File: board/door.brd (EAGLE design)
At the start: 28.8 x 37.5 mm, 15 parts, among them IC1 7805T

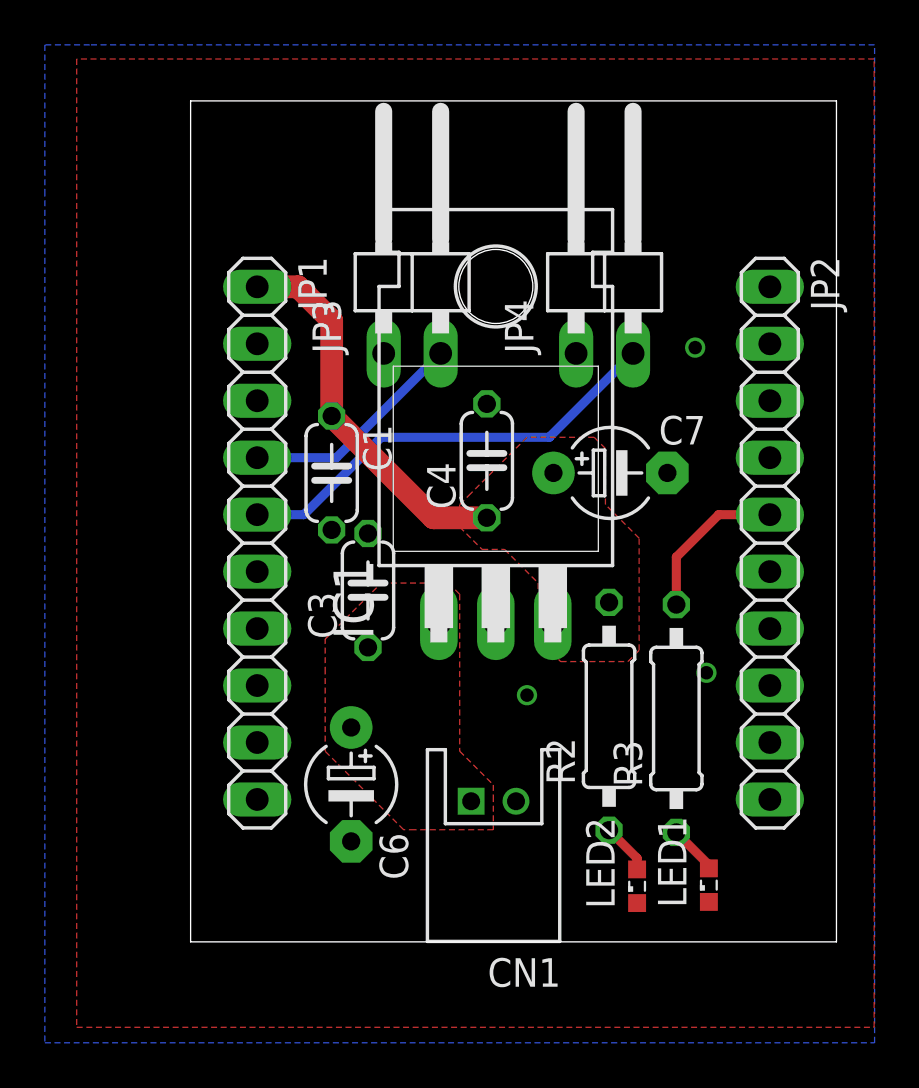
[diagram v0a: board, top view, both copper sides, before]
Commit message: add user_button
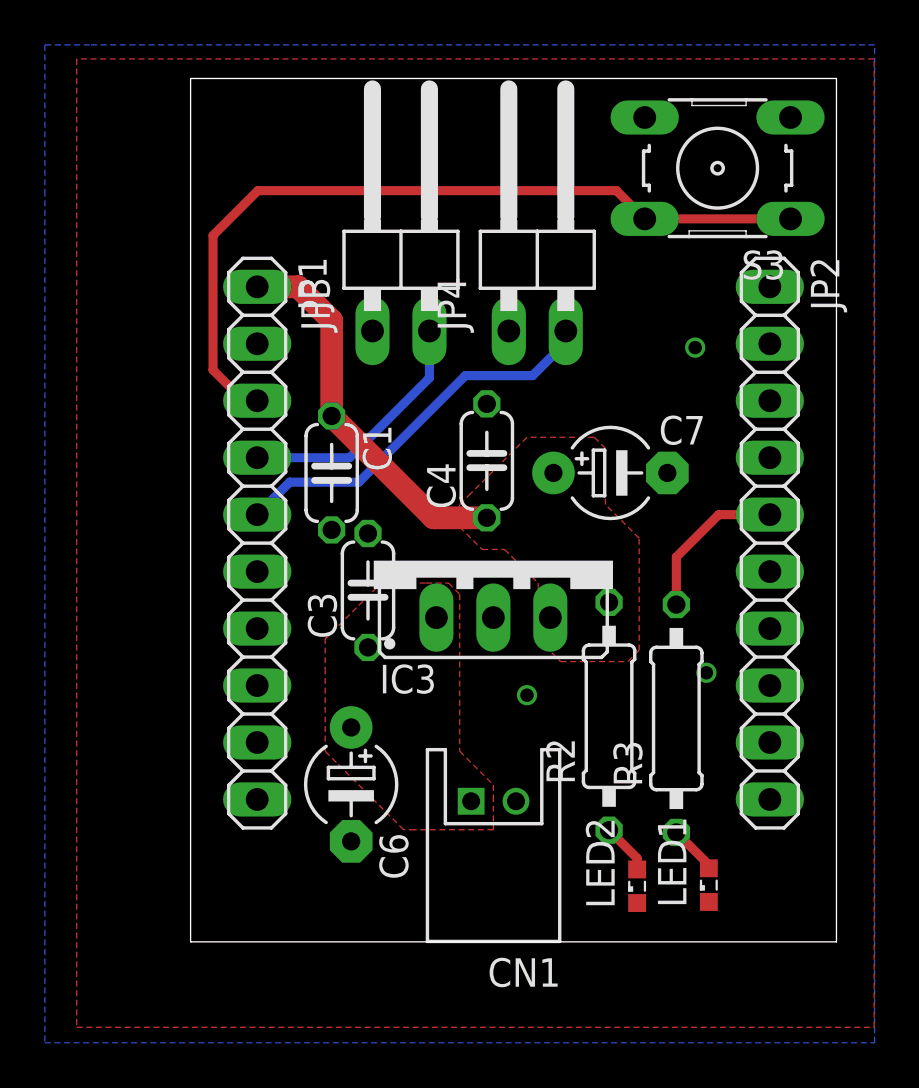
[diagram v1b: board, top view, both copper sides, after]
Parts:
- removed IC1: 7805T, linear4:TO220H
- added IC3: 7805, VoltageRegulator:TO220_V
- added S3: (no value), switch-omron:B3F-10XX
- moved JP4 3.16 mm to (15.5, 31.1)
- moved JP3 1.12 mm to (9.38, 31.1)
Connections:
- new net IO14: JP1.3, S3.1, S3.2
- net +3V3: now also IC3.3; no longer IC1.3
- net +8V: now also IC3.1; no longer IC1.1
- net GND: now also IC3.2, S3.3, S3.4; no longer IC1.2
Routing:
- net IO14: track 0.00 -> 35.6 mm
- net IO13: track 19.7 -> 17.5 mm
- net IO12: track 10.1 -> 11.2 mm
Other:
- board size 28.8 x 37.5 mm -> 28.8 x 38.5 mm
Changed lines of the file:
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@@
 <setting verticaltext="up"/>
 </settings>
-<grid distance="0.5" unitdist="mm" unit="mm" style="lines" multiple="1" display="no" altdistance="0.025" altunitdist="inch" altunit="inch"/>
+<grid distance="0.25" unitdist="mm" unit="mm" style="lines" multiple="1" display="no" altdistance="0.025" altunitdist="inch" altunit="inch"/>
 <layers>
 <layer number="1" name="Top" color="4" fill="1" visible="yes" active="yes"/>
@@
 <layer number="111" name="LPC17xx" color="7" fill="1" visible="yes" active="yes"/>
 <layer number="112" name="tSilk" color="7" fill="1" visible="yes" active="yes"/>
+<layer number="113" name="IDFDebug" color="7" fill="1" visible="yes" active="yes"/>
 <layer number="116" name="Patch_BOT" color="9" fill="4" visible="yes" active="yes"/>
 <layer number="118" name="Rect_Pads" color="7" fill="1" visible="no" active="no"/>
@@
 <plain>
 <wire x1="0" y1="0" x2="28.8" y2="0" width="0" layer="20"/>
-<wire x1="28.8" y1="0" x2="28.8" y2="37.5" width="0" layer="20"/>
-<wire x1="28.8" y1="37.5" x2="0" y2="37.5" width="0" layer="20"/>
-<wire x1="0" y1="37.5" x2="0" y2="0" width="0" layer="20"/>
+<wire x1="28.8" y1="0" x2="28.8" y2="38.5" width="0" layer="20"/>
+<wire x1="28.8" y1="38.5" x2="0" y2="38.5" width="0" layer="20"/>
+<wire x1="0" y1="38.5" x2="0" y2="0" width="0" layer="20"/>
 </plain>
 <attributes>
@@
 <element name="C7" library="rcl" package="E5-4" value="" x="18.72" y="20.91"/>
 <element name="CN1" library="jst-ph" package="S2B-PH-K-S" value="" x="13.51" y="6.27" rot="R180"/>
-<element name="IC1" library="linear4" package="TO220H" value="7805T" x="13.61" y="24.4"/>
 <element name="JP1" library="pinhead" package="1X10" value="" x="2.97" y="17.78" rot="R270"/>
 <element name="JP2" library="pinhead" package="1X10" value="" x="25.83" y="17.78" rot="R270"/>
-<element name="JP3" library="pinhead" package="1X02/90" value="" x="9.88" y="30.05"/>
-<element name="JP4" library="pinhead" package="1X02/90" value="" x="18.46" y="30.05"/>
+<element name="JP3" library="pinhead" package="1X02/90" value="" x="9.38" y="31.05"/>
+<element name="JP4" library="pinhead" package="1X02/90" value="" x="15.46" y="31.05"/>
 <element name="LED1" library="led" package="SML0603" value="" x="23.11" y="2.53" rot="R90"/>
 <element name="LED2" library="led" package="SML0603" value="" x="19.91" y="2.48" rot="R90"/>
 <element name="R2" library="rcl" package="0207/10" value="1k" x="18.66" y="10.06" rot="R90"/>
 <element name="R3" library="rcl" package="0207/10" value="1k" x="21.66" y="9.96" rot="R90"/>
+<element name="S3" library="switch-omron" package="B3F-10XX" value="" x="23.5" y="34.5" rot="R180">
+<attribute name="MPN" value="B3F-1000" x="23.5" y="34.5" size="1.778" layer="27" rot="R180" display="off"/>
+<attribute name="MF" value="" x="23.5" y="34.5" size="1.778" layer="27" rot="R180" display="off"/>
+<attribute name="OC_NEWARK" value="36M3542" x="23.5" y="34.5" size="1.778" layer="27" rot="R180" display="off"/>
+<attribute name="OC_FARNELL" value="176432" x="23.5" y="34.5" size="1.778" layer="27" rot="R180" display="off"/>
+</element>
+<element name="IC3" library="VoltageRegulator" package="TO220_V" value="7805" x="13.5" y="17"/>
 </elements>
 <signals>
 <signal name="+8V">
 <contactref element="CN1" pad="1"/>
-<contactref element="IC1" pad="1"/>
 <contactref element="C3" pad="1"/>
 <contactref element="C6" pad="+"/>
@@
 <vertex x="13.5" y="7"/>
 </polygon>
+<contactref element="IC3" pad="1"/>
 </signal>
 <signal name="GND">
 <contactref element="CN1" pad="2"/>
-<contactref element="IC1" pad="2"/>
 <contactref element="C3" pad="2"/>
 <contactref element="C4" pad="2"/>
@@
 <vertex x="-6.5" y="40"/>
 </polygon>
+<contactref element="S3" pad="3"/>
+<contactref element="S3" pad="4"/>
+<contactref element="IC3" pad="2"/>
 </signal>
 <signal name="+3V3">
-<contactref element="IC1" pad="3"/>
 <contactref element="C4" pad="1"/>
 <contactref element="C7" pad="+"/>
@@
 <wire x1="13.21" y1="18.91" x2="10.83" y2="18.91" width="1.016" layer="1"/>
 <wire x1="10.83" y1="18.91" x2="6.29" y2="23.45" width="1.016" layer="1"/>
+<contactref element="IC3" pad="3"/>
 </signal>
 <signal name="A" class="1">
@@
 <contactref element="JP1" pad="4"/>
 <contactref element="JP3" pad="2"/>
-<wire x1="2.97" y1="21.59" x2="6.5" y2="21.59" width="0.4064" layer="16"/>
-<wire x1="6.5" y1="21.59" x2="11.15" y2="26.24" width="0.4064" layer="16"/>
+<wire x1="2.97" y1="21.59" x2="7.09" y2="21.59" width="0.4064" layer="16"/>
+<wire x1="7.09" y1="21.59" x2="10.65" y2="25.15" width="0.4064" layer="16"/>
+<wire x1="10.65" y1="25.15" x2="10.65" y2="27.24" width="0.4064" layer="16"/>
 </signal>
 <signal name="IO13">
 <contactref element="JP1" pad="5"/>
 <contactref element="JP4" pad="2"/>
-<wire x1="2.97" y1="19.05" x2="5.05" y2="19.05" width="0.4064" layer="16"/>
-<wire x1="5.05" y1="19.05" x2="8.5" y2="22.5" width="0.4064" layer="16"/>
-<wire x1="8.5" y1="22.5" x2="16" y2="22.5" width="0.4064" layer="16"/>
-<wire x1="16" y1="22.5" x2="16" y2="22.51" width="0.4064" layer="16"/>
-<wire x1="16" y1="22.51" x2="19.73" y2="26.24" width="0.4064" layer="16"/>
+<wire x1="2.97" y1="19.05" x2="4.42" y2="20.5" width="0.4064" layer="16"/>
+<wire x1="4.42" y1="20.5" x2="7.5" y2="20.5" width="0.4064" layer="16"/>
+<wire x1="7.5" y1="20.5" x2="12.25" y2="25.25" width="0.4064" layer="16"/>
+<wire x1="12.25" y1="25.25" x2="15.25" y2="25.25" width="0.4064" layer="16"/>
+<wire x1="15.25" y1="25.25" x2="16.73" y2="26.73" width="0.4064" layer="16"/>
+<wire x1="16.73" y1="26.73" x2="16.73" y2="27.24" width="0.4064" layer="16"/>
+</signal>
+<signal name="IO14">
+<contactref element="JP1" pad="3"/>
+<contactref element="S3" pad="1"/>
+<contactref element="S3" pad="2"/>
+<wire x1="2.97" y1="24.13" x2="2.37" y2="24.13" width="0.4064" layer="1"/>
+<wire x1="2.37" y1="24.13" x2="1" y2="25.5" width="0.4064" layer="1"/>
+<wire x1="1" y1="25.5" x2="1" y2="31.5" width="0.4064" layer="1"/>
+<wire x1="1" y1="31.5" x2="3" y2="33.5" width="0.4064" layer="1"/>
+<wire x1="3" y1="33.5" x2="18.9882" y2="33.5" width="0.4064" layer="1"/>
+<wire x1="18.9882" y1="33.5" x2="20.2488" y2="32.2394" width="0.4064" layer="1"/>
+<wire x1="20.2488" y1="32.2394" x2="26.7512" y2="32.2394" width="0.4064" layer="1"/>
 </signal>
 </signals>
